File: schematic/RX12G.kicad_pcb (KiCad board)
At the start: 4 copper layers, 40 x 35 mm, 43 parts, among them J1 ICSP, J2 TSW-104-08-G-T-RA, J3 TSW-104-08-G-T-RA, J4 TSW-104-08-G-T-RA, J5 Conn_01x03, J6 Conn_01x03, J7 USB_B_Micro, J8 Conn_01x03, Q1 2N7002P_215, SW1 SW_MEC_5E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

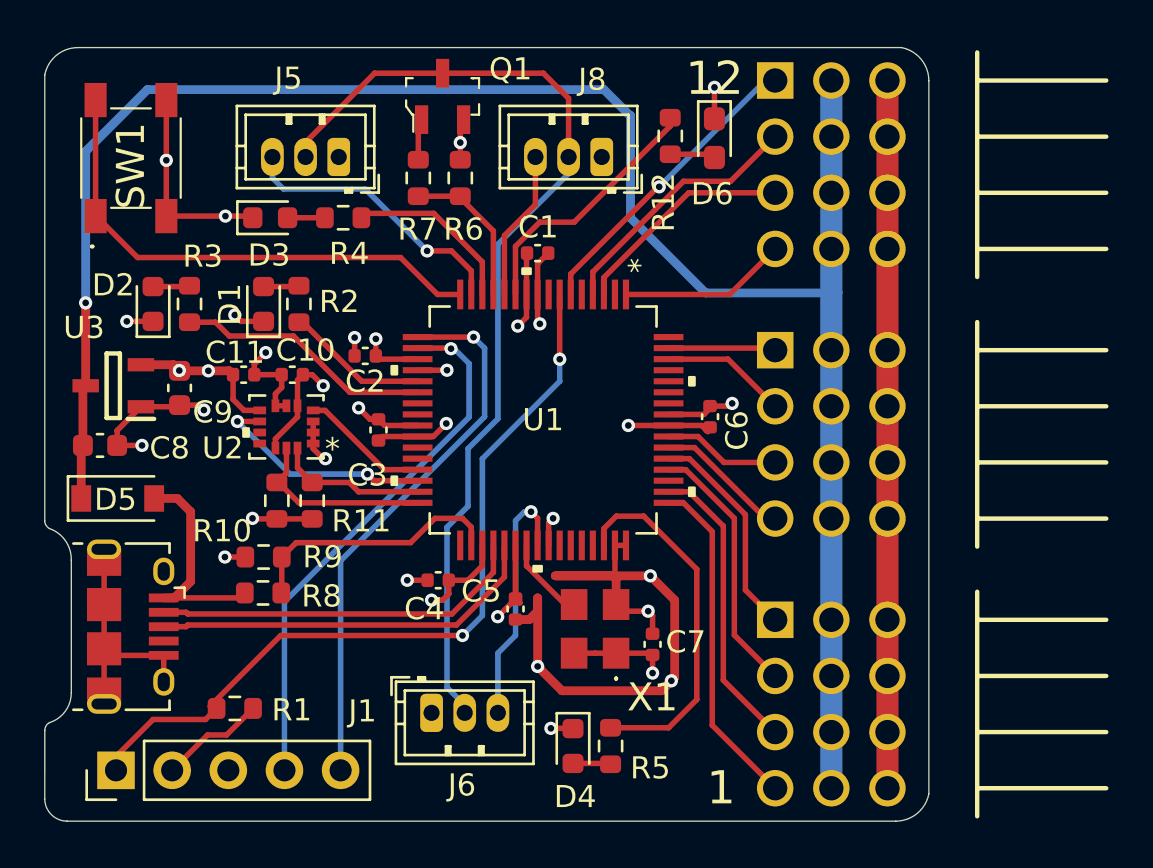
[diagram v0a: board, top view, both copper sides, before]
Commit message: Repositioned some components
Moved sat leds, hid the connector labels
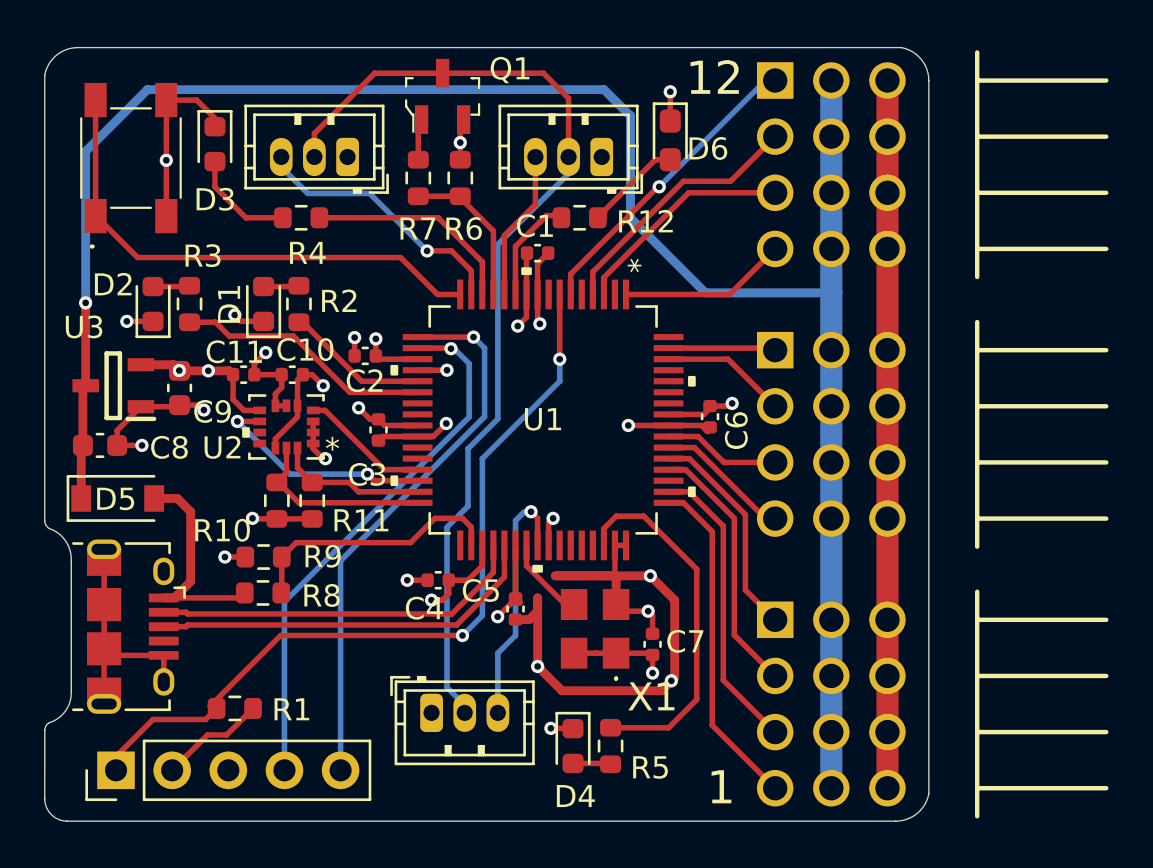
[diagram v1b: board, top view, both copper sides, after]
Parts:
- moved R12 5.52 mm to (143.2, 99.7), turned to 0 degrees
- moved D3 4.16 mm to (126.7, 96.4), turned to -90 degrees
- moved D6 2.00 mm to (147.3, 96.2)
- moved R4 1.90 mm to (130.6, 99.7)
- moved J5 0.40 mm to (132.7, 97.0)
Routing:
- net LED_SAT3: track 11.8 -> 4.87 mm
- net Net-(D3-Pad2): track 1.69 -> 4.80 mm
- net Net-(D6-Pad2): track 2.06 -> 4.25 mm
- net LED_SAT1: track 7.86 -> 9.67 mm
- net GND: track 115.4 -> 114.4 mm, vias 23 -> 22
- net SAT1_RX: track 13.0 -> 12.1 mm

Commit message: Minor fixes.
D6 footprint, updated BOM
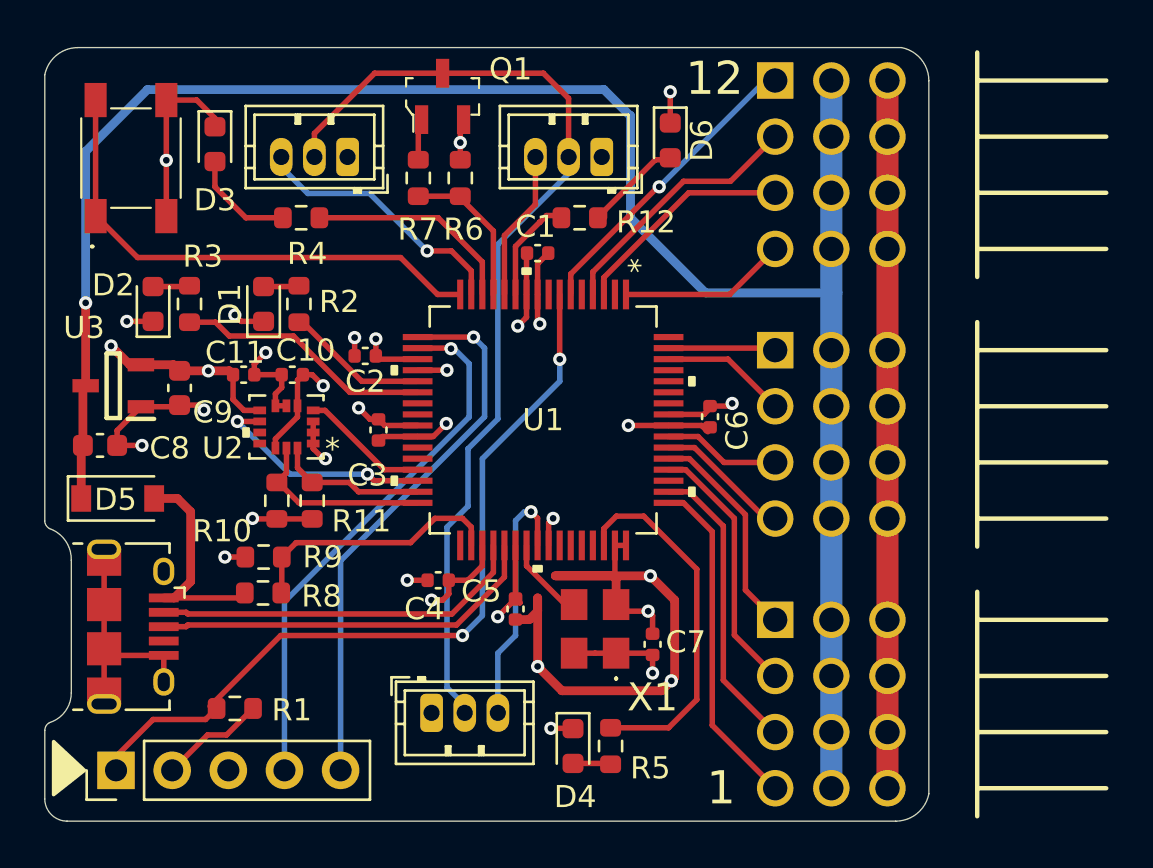
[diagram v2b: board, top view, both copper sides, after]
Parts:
- D6: footprint LED_SMD:LED_0603_1608Metric_Pad1.05x0.95mm_HandSolder -> LED_SMD:LED_0603_1608Metric
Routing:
- net +3V3: track 44.4 -> 46.1 mm
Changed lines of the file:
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@@
 (kicad_pcb (version 20211014) (generator pcbnew)
   (general
-    (thickness 4.69)
+    (thickness 1.6)
   )
   (paper "A4")
@@
       (layer "F.Mask" (type "Top Solder Mask") (color "Blue") (thickness 0.01))
       (layer "F.Cu" (type "copper") (thickness 0.035))
-      (layer "dielectric 1" (type "core") (thickness 1.51) (material "FR4") (epsilon_r 4.5) (loss_tangent 0.02))
+      (layer "dielectric 1" (type "core") (thickness 0.48) (material "FR4") (epsilon_r 4.5) (loss_tangent 0.02))
       (layer "In1.Cu" (type "copper") (thickness 0.035))
-      (layer "dielectric 2" (type "prepreg") (thickness 1.51) (material "FR4") (epsilon_r 4.5) (loss_tangent 0.02))
+      (layer "dielectric 2" (type "prepreg") (thickness 0.48) (material "FR4") (epsilon_r 4.5) (loss_tangent 0.02))
       (layer "In2.Cu" (type "copper") (thickness 0.035))
-      (layer "dielectric 3" (type "core") (thickness 1.51) (material "FR4") (epsilon_r 4.5) (loss_tangent 0.02))
+      (layer "dielectric 3" (type "core") (thickness 0.48) (material "FR4") (epsilon_r 4.5) (loss_tangent 0.02))
       (layer "B.Cu" (type "copper") (thickness 0.035))
       (layer "B.Mask" (type "Bottom Solder Mask") (color "Blue") (thickness 0.01))
@@
     )
   )
-  (footprint "LED_SMD:LED_0603_1608Metric_Pad1.05x0.95mm_HandSolder" (layer "F.Cu")
+  (footprint "LED_SMD:LED_0603_1608Metric" (layer "F.Cu")
     (at 147.3 96.2 -90)
     (descr "LED SMD 0603 (1608 Metric), square (rectangular) end terminal, IPC_7351 nominal, (Body size source: http://www.tortai-tech.com/upload/download/2011102023233369053.pdf), generated with kicad-footprint-generator")
-    (tags "LED handsolder")
+    (tags "LED")
     (property "Sheetfile" "power.kicad_sch")
     (property "Sheetname" "Power, LEDs, IMU and Button")
     (attr smd)
-    (fp_text reference "D6" (at 0.4 -1.7) (layer "F.SilkS")
-      (effects (font (size 1 1) (thickness 0.15)))
-    )
-    (fp_text value "LED" (at 0 1.43 90) (layer "F.Fab")
-      (effects (font (size 1 1) (thickness 0.15)))
-    )
-    (fp_text user "${REFERENCE}" (at 0 0 90) (layer "F.Fab")
+    (fp_text reference "D6" (at 0 -1.43 -90) (layer "F.SilkS")
+      (effects (font (size 1 1) (thickness 0.15)))
+    )
+    (fp_text value "LED" (at 0 1.43 -90) (layer "F.Fab")
+      (effects (font (size 1 1) (thickness 0.15)))
+    )
+    (fp_text user "${REFERENCE}" (at 0 0 -90) (layer "F.Fab")
       (effects (font (size 0.4 0.4) (thickness 0.06)))
     )
-    (fp_line (start -1.66 0.735) (end 0.8 0.735) (layer "F.SilkS") (width 0.12))
-    (fp_line (start -1.66 -0.735) (end -1.66 0.735) (layer "F.SilkS") (width 0.12))
-    (fp_line (start 0.8 -0.735) (end -1.66 -0.735) (layer "F.SilkS") (width 0.12))
-    (fp_line (start -1.65 0.73) (end -1.65 -0.73) (layer "F.CrtYd") (width 0.05))
-    (fp_line (start -1.65 -0.73) (end 1.65 -0.73) (layer "F.CrtYd") (width 0.05))
-    (fp_line (start 1.65 0.73) (end -1.65 0.73) (layer "F.CrtYd") (width 0.05))
-    (fp_line (start 1.65 -0.73) (end 1.65 0.73) (layer "F.CrtYd") (width 0.05))
-    (fp_line (start -0.8 0.4) (end 0.8 0.4) (layer "F.Fab") (width 0.1))
+    (fp_line (start -1.485 -0.735) (end -1.485 0.735) (layer "F.SilkS") (width 0.12))
+    (fp_line (start -1.485 0.735) (end 0.8 0.735) (layer "F.SilkS") (width 0.12))
+    (fp_line (start 0.8 -0.735) (end -1.485 -0.735) (layer "F.SilkS") (width 0.12))
+    (fp_line (start 1.48 0.73) (end -1.48 0.73) (layer "F.CrtYd") (width 0.05))
+    (fp_line (start -1.48 -0.73) (end 1.48 -0.73) (layer "F.CrtYd") (width 0.05))
+    (fp_line (start -1.48 0.73) (end -1.48 -0.73) (layer "F.CrtYd") (width 0.05))
+    (fp_line (start 1.48 -0.73) (end 1.48 0.73) (layer "F.CrtYd") (width 0.05))
+    (fp_line (start -0.8 -0.1) (end -0.8 0.4) (layer "F.Fab") (width 0.1))
     (fp_line (start 0.8 0.4) (end 0.8 -0.4) (layer "F.Fab") (width 0.1))
     (fp_line (start -0.5 -0.4) (end -0.8 -0.1) (layer "F.Fab") (width 0.1))
     (fp_line (start 0.8 -0.4) (end -0.5 -0.4) (layer "F.Fab") (width 0.1))
-    (fp_line (start -0.8 -0.1) (end -0.8 0.4) (layer "F.Fab") (width 0.1))
-    (pad "1" smd roundrect locked (at -0.875 0 270) (size 1.05 0.95) (layers "F.Cu" "F.Paste" "F.Mask") (roundrect_rratio 0.25)
+    (fp_line (start -0.8 0.4) (end 0.8 0.4) (layer "F.Fab") (width 0.1))
+    (pad "1" smd roundrect locked (at -0.7875 0 270) (size 0.875 0.95) (layers "F.Cu" "F.Paste" "F.Mask") (roundrect_rratio 0.25)
       (net 2 "GND") (pinfunction "K") (pintype "passive"))
-    (pad "2" smd roundrect locked (at 0.875 0 270) (size 1.05 0.95) (layers "F.Cu" "F.Paste" "F.Mask") (roundrect_rratio 0.25)
+    (pad "2" smd roundrect locked (at 0.7875 0 270) (size 0.875 0.95) (layers "F.Cu" "F.Paste" "F.Mask") (roundrect_rratio 0.25)
       (net 9 "Net-(D6-Pad2)") (pinfunction "A") (pintype "passive"))
     (model "${KICAD6_3DMODEL_DIR}/LED_SMD.3dshapes/LED_0603_1608Metric.wrl"
@@
       (xy 119.502208 123.448265)
     ) (layer "B.SilkS") (width 0.16) (fill solid))
+  (gr_poly
+    (pts
+      (xy 120.795 124.7)
+      (xy 119.4 125.8)
+      (xy 119.4 123.4)
+    ) (layer "F.SilkS") (width 0.16) (fill solid))
   (gr_arc (start 119.21 113.76) (mid 119.941156 114.317643) (end 120.2 115.2) (layer "Edge.Cuts") (width 0.05))
   (gr_line (start 120.007107 127) (end 157.5 127) (layer "Edge.Cuts") (width 0.05))
@@
   (segment (start 129.435001 110.1213) (end 129.435001 109.708219) (width 0.25) (layer "F.Cu") (net 1))
   (segment (start 125.1 106.625) (end 127.345 106.625) (width 0.4) (layer "F.Cu") (net 1))
+  (segment (start 122.85 106.35) (end 122 105.5) (width 0.4) (layer "F.Cu") (net 1))
   (segment (start 130.434999 108.2087) (end 130.434999 107.045001) (width 0.25) (layer "F.Cu") (net 1))
   (segment (start 147.2244 108.5975) (end 148.8225 108.5975) (width 0.25) (layer "F.Cu") (net 1))
@@
   (segment (start 136.577891 109.597501) (end 137.167267 109.008125) (width 0.25) (layer "F.Cu") (net 1))
   (segment (start 127.345 106.625) (end 127.52 106.8) (width 0.4) (layer "F.Cu") (net 1))
+  (segment (start 123.35 106.35) (end 122.85 106.35) (width 0.4) (layer "F.Cu") (net 1))
   (segment (start 140.5 117.12) (end 140.121756 117.12) (width 0.25) (layer "F.Cu") (net 1))
   (segment (start 146.5 119.48) (end 146.5 120.3) (width 0.25) (layer "F.Cu") (net 1))
@@
   (via (at 137.167267 109.008125) (size 0.6) (drill 0.3) (layers "F.Cu" "B.Cu") (net 1))
   (via (at 136.5 117) (size 0.6) (drill 0.3) (layers "F.Cu" "B.Cu") (net 1))
+  (via (at 122 105.5) (size 0.6) (drill 0.3) (layers "F.Cu" "B.Cu") (net 1))
   (via (at 139.492203 117.749553) (size 0.6) (drill 0.3) (layers "F.Cu" "B.Cu") (net 1))
   (via (at 150.1 108.1) (size 0.6) (drill 0.3) (layers "F.Cu" "B.Cu") (net 1))
   (via (at 133.98 105.18) (size 0.6) (drill 0.3) (layers "F.Cu" "B.Cu") (net 1))
-  (via (at 125.0875 106.6125) (size 0.6) (drill 0.3) (layers "F.Cu" "B.Cu") (net 1))
   (via (at 131.6 107.3) (size 0.6) (drill 0.3) (layers "F.Cu" "B.Cu") (net 1))
   (via (at 140.4 104.6) (size 0.6) (drill 0.3) (layers "F.Cu" "B.Cu") (net 1))

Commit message: Some minor silkscreen fixes
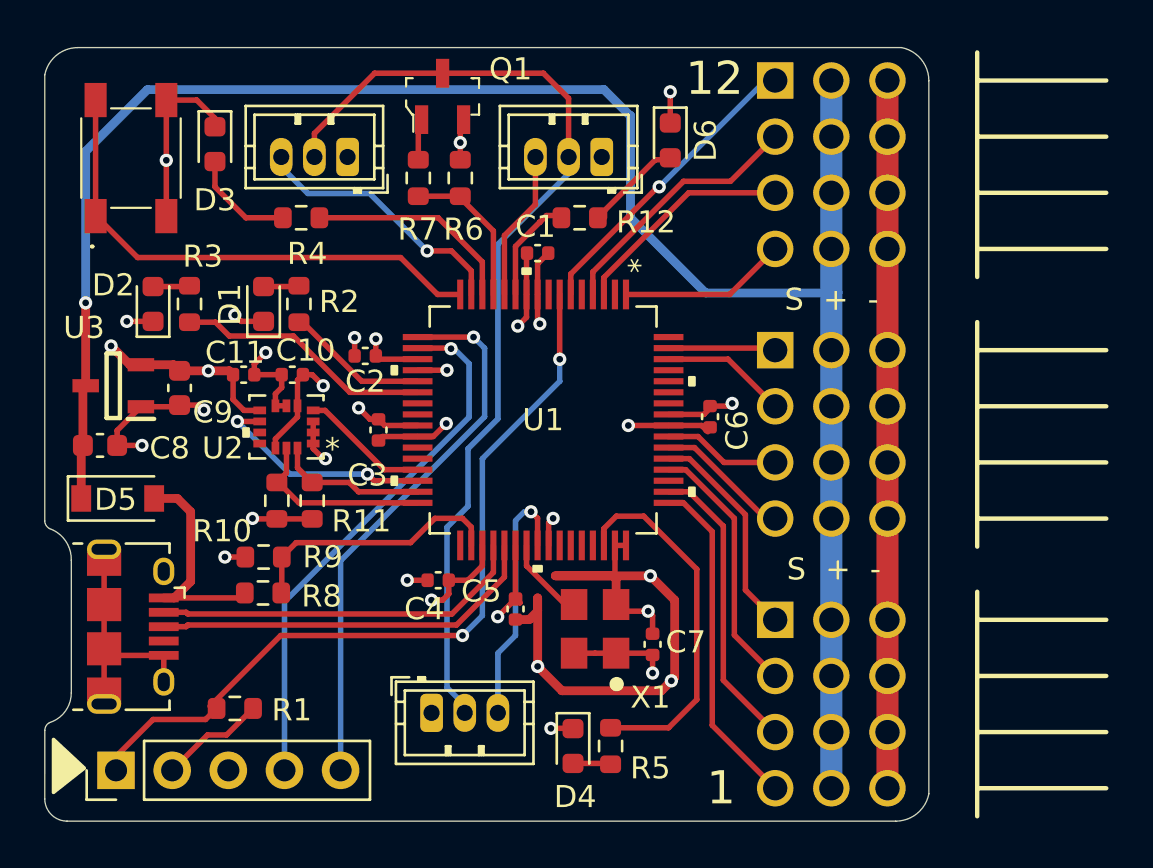
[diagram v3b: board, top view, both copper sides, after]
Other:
- board text added: "S + -"
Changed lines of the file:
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@@
     (property "Sheetname" "")
     (attr smd)
-    (fp_text reference "X1" (at -3.1 2.6 180) (layer "F.SilkS")
-      (effects (font (size 1.27 1.27) (thickness 0.254)))
-    )
-    (fp_text value "24 MHz" (at 0 0 90) (layer "F.SilkS") hide
+    (fp_text reference "X1" (at -3.1 2.5 180) (layer "F.SilkS")
+      (effects (font (size 1 1) (thickness 0.15)))
+    )
+    (fp_text value "24 MHz" (at -0.175 -0.4 90) (layer "F.SilkS") hide
       (effects (font (size 1.27 1.27) (thickness 0.254)))
     )
@@
       (effects (font (size 1.27 1.27) (thickness 0.254)))
     )
-    (fp_line (start -2.3 0.95) (end -2.3 0.95) (layer "F.SilkS") (width 0.1))
-    (fp_line (start -2.2 0.95) (end -2.2 0.95) (layer "F.SilkS") (width 0.1))
-    (fp_arc (start -2.2 0.95) (mid -2.25 1) (end -2.3 0.95) (layer "F.SilkS") (width 0.1))
-    (fp_arc (start -2.3 0.95) (mid -2.25 0.9) (end -2.2 0.95) (layer "F.SilkS") (width 0.1))
+    (fp_circle (center -2.5 0.975) (end -2.234246 0.975) (layer "F.SilkS") (width 0.12) (fill solid))
     (fp_rect (start 2.05 1.825) (end -2.1 -1.875) (layer "F.CrtYd") (width 0.12) (fill none))
     (fp_line (start -1.6 -1.25) (end 1.6 -1.25) (layer "F.Fab") (width 0.1))
@@
     (property "Sheetname" "Power, LEDs, IMU and Button")
     (attr smd)
-    (fp_text reference "D6" (at 0 -1.43 -90) (layer "F.SilkS")
+    (fp_text reference "D6" (at 0 -1.6 -90) (layer "F.SilkS")
       (effects (font (size 1 1) (thickness 0.15)))
     )
@@
   (gr_poly
     (pts
-      (xy 120.795 124.7)
-      (xy 119.4 125.8)
-      (xy 119.4 123.4)
+      (xy 120.790202 124.6)
+      (xy 119.395202 125.7)
+      (xy 119.395202 123.3)
     ) (layer "F.SilkS") (width 0.16) (fill solid))
   (gr_arc (start 119.21 113.76) (mid 119.941156 114.317643) (end 120.2 115.2) (layer "Edge.Cuts") (width 0.05))
@@
     (effects (font (size 2 2) (thickness 0.2)) (justify left mirror))
   )
-  (gr_text "JLCJLCJLCJLC" (at 141.7 126.1) (layer "B.SilkS")
+  (gr_text "JLCJLCJLCJLC" (at 139.6 126) (layer "B.SilkS")
     (effects (font (size 1 1) (thickness 0.16)) (justify mirror))
   )
@@
     (effects (font (size 1 1) (thickness 0.16)) (justify mirror))
   )
-  (gr_text "-  +  S" (at 154.6 115.5) (layer "B.SilkS")
-    (effects (font (size 1 1) (thickness 0.16)) (justify mirror))
-  )
   (gr_text "12" (at 149.3 93.4) (layer "B.SilkS")
     (effects (font (size 1.5 1.5) (thickness 0.2)) (justify mirror))
   )
+  (gr_text "-  +  S" (at 154.6 115.6) (layer "B.SilkS")
+    (effects (font (size 1 1) (thickness 0.16)) (justify mirror))
+  )
+  (gr_text "S  +  -" (at 154.7 115.6) (layer "F.SilkS")
+    (effects (font (size 1 1) (thickness 0.16)))
+  )
   (gr_text "1" (at 149.6 125.5) (layer "F.SilkS")
     (effects (font (size 1.5 1.5) (thickness 0.2)))
   )
+  (gr_text "S  +  -" (at 154.6 103.4) (layer "F.SilkS")
+    (effects (font (size 1 1) (thickness 0.16)))
+  )
   (gr_text "12" (at 149.3 93.4) (layer "F.SilkS")

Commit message: Changed R3 value and some minor track adjustments
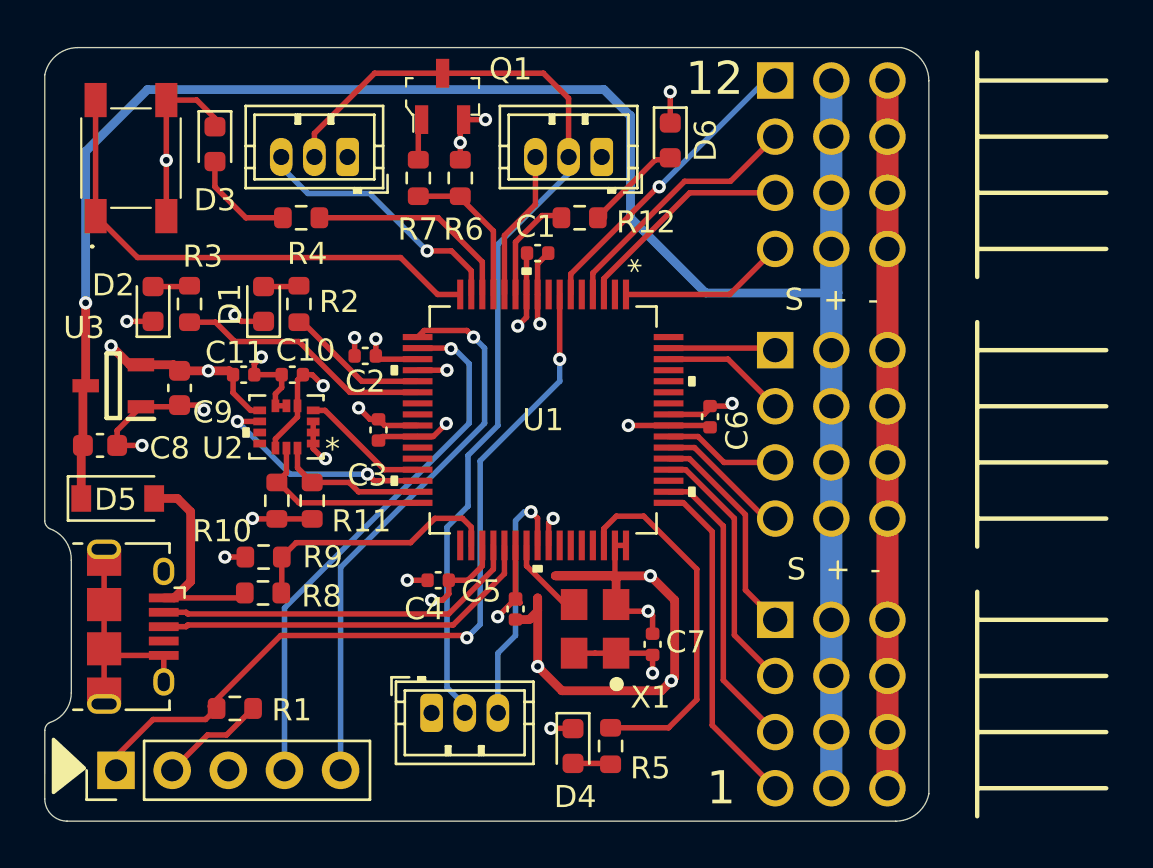
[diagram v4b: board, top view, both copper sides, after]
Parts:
- R3: value 62R -> 56R
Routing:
- net GND: track 114.4 -> 115.1 mm, vias 22 -> 23
